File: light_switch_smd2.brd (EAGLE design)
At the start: 36.6 x 44.7 mm, 17 parts, among them J2 SW1, T1 BT136, U1 LM1117

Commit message: version 3, several correction added
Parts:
- AC: value (none) -> AC
- LAMP: value (none) -> LAMP
- moved LAMP 2.00 mm to (31.0, 42.0)
- moved AC 1.50 mm to (0.80, 41.9)
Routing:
- net N$11: track 49.5 -> 52.1 mm
- net N$8: track 36.3 -> 38.3 mm
- net GND: track 73.0 -> 73.5 mm
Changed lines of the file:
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@@
 <grid distance="0.5" unitdist="mm" unit="mm" style="lines" multiple="1" display="yes" altdistance="0.25" altunitdist="mm" altunit="mm"/>
 <layers>
-<layer number="1" name="Top" color="4" fill="1" visible="no" active="yes"/>
-<layer number="16" name="Bottom" color="1" fill="1" visible="no" active="yes"/>
+<layer number="1" name="Top" color="4" fill="1" visible="yes" active="yes"/>
+<layer number="16" name="Bottom" color="1" fill="1" visible="yes" active="yes"/>
 <layer number="17" name="Pads" color="2" fill="1" visible="yes" active="yes"/>
 <layer number="18" name="Vias" color="2" fill="1" visible="yes" active="yes"/>
@@
 <attribute name="PROD_ID" value="VREG-08170" x="12.58" y="32.06" size="1.778" layer="27" display="off"/>
 </element>
-<element name="LAMP" library="SparkFun-Connectors" package="1X03_NO_SILK" value="" x="29" y="42"/>
-<element name="AC" library="SparkFun-Connectors" package="1X03_NO_SILK" value="" x="2.3" y="41.9"/>
+<element name="LAMP" library="SparkFun-Connectors" package="1X03_NO_SILK" value="LAMP" x="31" y="42"/>
+<element name="AC" library="SparkFun-Connectors" package="1X03_NO_SILK" value="AC" x="0.8" y="41.9"/>
 </elements>
 <signals>
@@
 <wire x1="2" y1="19.4" x2="2" y2="16.21" width="0.4064" layer="16"/>
 <wire x1="2" y1="16.21" x2="2.02" y2="16.19" width="0.4064" layer="16"/>
-<wire x1="33.49" y1="3.77" x2="33.49" y2="14.21" width="0.4064" layer="16"/>
+<wire x1="33.49" y1="3.27" x2="33.49" y2="14.21" width="0.4064" layer="16"/>
 <wire x1="33.49" y1="14.21" x2="25" y2="22.7" width="0.4064" layer="16"/>
 <wire x1="25" y1="22.7" x2="8.3" y2="22.7" width="0.4064" layer="16"/>
@@
 <wire x1="23.61" y1="38.92" x2="23.61" y2="40.21" width="0.4064" layer="16"/>
 <wire x1="23.61" y1="40.21" x2="25.4" y2="42" width="0.4064" layer="16"/>
-<wire x1="25.4" y1="42" x2="29" y2="42" width="0.4064" layer="16"/>
+<wire x1="25.4" y1="42" x2="31" y2="42" width="0.4064" layer="16"/>
 </signal>
 <signal name="N$11">
@@
 <contactref element="LAMP" pad="3"/>
 <contactref element="AC" pad="1"/>
-<wire x1="2.3" y1="41.9" x2="2.3" y2="40.5" width="0.4064" layer="16"/>
-<wire x1="2.3" y1="40.5" x2="1.2" y2="39.4" width="0.4064" layer="16"/>
+<wire x1="0.8" y1="41.9" x2="0.8" y2="40.5" width="0.4064" layer="16"/>
+<wire x1="0.8" y1="40.5" x2="1.2" y2="39.4" width="0.4064" layer="16"/>
 <wire x1="1.2" y1="39.4" x2="1.2" y2="35.5" width="0.4064" layer="16"/>
 <wire x1="1.2" y1="35.5" x2="2.5" y2="34.2" width="0.4064" layer="16"/>
 <wire x1="2.5" y1="34.2" x2="23.85" y2="34.2" width="0.4064" layer="16"/>
-<wire x1="23.85" y1="34.2" x2="23.94" y2="34.29" width="0.4064" layer="16"/>
-<wire x1="23.94" y1="34.29" x2="23.94" y2="34.26" width="0.4064" layer="16"/>
-<wire x1="23.94" y1="34.26" x2="26.2" y2="32" width="0.4064" layer="16"/>
-<wire x1="26.2" y1="32" x2="31.1" y2="32" width="0.4064" layer="16"/>
-<wire x1="31.1" y1="32" x2="34.1" y2="35" width="0.4064" layer="16"/>
-<wire x1="34.1" y1="35" x2="34.1" y2="41.98" width="0.4064" layer="16"/>
-<wire x1="34.1" y1="41.98" x2="34.08" y2="42" width="0.4064" layer="16"/>
+<wire x1="23.85" y1="34.2" x2="23.94" y2="34.79" width="0.4064" layer="16"/>
+<wire x1="23.94" y1="34.79" x2="23.94" y2="33.56" width="0.4064" layer="16"/>
+<wire x1="23.94" y1="33.56" x2="26.5" y2="31" width="0.4064" layer="16"/>
+<wire x1="26.5" y1="31" x2="30" y2="31" width="0.4064" layer="16"/>
+<wire x1="30" y1="31" x2="36" y2="37" width="0.4064" layer="16"/>
+<wire x1="36" y1="37" x2="36" y2="41.92" width="0.4064" layer="16"/>
+<wire x1="36" y1="41.92" x2="36.08" y2="42" width="0.4064" layer="16"/>
 </signal>
 <signal name="N$12">
@@
 <contactref element="U$1" pad="AC1"/>
 <contactref element="AC" pad="3"/>
-<wire x1="28.42" y1="34.29" x2="28.42" y2="36.65" width="0.4064" layer="16"/>
+<wire x1="28.42" y1="34.79" x2="28.42" y2="36.65" width="0.4064" layer="16"/>
 <wire x1="28.42" y1="36.65" x2="26.15" y2="38.92" width="0.4064" layer="16"/>
-<wire x1="7.38" y1="41.9" x2="10.1" y2="41.9" width="0.4064" layer="1"/>
-<wire x1="10.1" y1="41.9" x2="16.3" y2="35.7" width="0.4064" layer="1"/>
-<wire x1="16.3" y1="35.7" x2="25" y2="35.7" width="0.4064" layer="1"/>
-<wire x1="25" y1="35.7" x2="26.2" y2="36.9" width="0.4064" layer="1"/>
+<wire x1="5.88" y1="41.9" x2="10.1" y2="41.9" width="0.4064" layer="1"/>
+<wire x1="10.1" y1="41.9" x2="16.3" y2="36.2" width="0.4064" layer="1"/>
+<wire x1="16.3" y1="36.2" x2="25" y2="36.2" width="0.4064" layer="1"/>
+<wire x1="25" y1="36.2" x2="26.2" y2="36.9" width="0.4064" layer="1"/>
 <wire x1="26.2" y1="36.9" x2="26.2" y2="38.87" width="0.4064" layer="1"/>
 <wire x1="26.2" y1="38.87" x2="26.15" y2="38.92" width="0.4064" layer="1"/>
@@
 <wire x1="14.23" y1="25.17" x2="18.9" y2="20.5" width="0.4064" layer="1"/>
 <wire x1="18.9" y1="20.5" x2="18.9" y2="3.77" width="0.4064" layer="1"/>
-<wire x1="18.9" y1="3.77" x2="18.88" y2="3.75" width="0.4064" layer="1"/>
+<wire x1="18.9" y1="3.77" x2="18.88" y2="3.25" width="0.4064" layer="1"/>
 </signal>
 <signal name="N$1">

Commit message: More minor corrections.
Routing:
- net N$17: track 8.90 -> 0.00 mm
- net GND: track 73.5 -> 66.2 mm
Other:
- board text added: "Hristo Borisov Light Switch Prototype Rev. 0.3"
- board text removed: "Hristo Borisov Light Switch Rev. 0.1 Prototype"
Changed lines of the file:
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@@
 <setting verticaltext="up"/>
 </settings>
-<grid distance="0.5" unitdist="mm" unit="mm" style="lines" multiple="1" display="yes" altdistance="0.25" altunitdist="mm" altunit="mm"/>
+<grid distance="0.1" unitdist="mm" unit="mm" style="lines" multiple="1" display="yes" altdistance="0.01" altunitdist="mm" altunit="mm"/>
 <layers>
-<layer number="1" name="Top" color="4" fill="1" visible="yes" active="yes"/>
+<layer number="1" name="Top" color="4" fill="1" visible="no" active="yes"/>
 <layer number="16" name="Bottom" color="1" fill="1" visible="yes" active="yes"/>
 <layer number="17" name="Pads" color="2" fill="1" visible="yes" active="yes"/>
@@
 <wire x1="36.6" y1="43.7" x2="0.1" y2="43.7" width="0" layer="20"/>
 <wire x1="0.1" y1="43.7" x2="0" y2="-1" width="0" layer="20"/>
-<dimension x1="0.1" y1="-1" x2="36.7" y2="-1" x3="18.4" y3="-5.4" textsize="1.778" layer="16"/>
-<text x="23.3" y="5.4" size="1.778" layer="16" rot="MR90">Hristo Borisov
-Light Switch
-Rev. 0.1 Prototype</text>
 <hole x="17.4" y="41" drill="3.2"/>
 <hole x="18.3" y="0.8" drill="3.2"/>
+<text x="32" y="26" size="1.778" layer="16" rot="MR270">Hristo Borisov
+Light Switch
+Prototype
+Rev. 0.3</text>
 </plain>
 <attributes>
@@
 <wire x1="11.18" y1="22.67" x2="8.33" y2="22.67" width="0.4064" layer="1"/>
 <wire x1="8.33" y1="22.67" x2="8.2" y2="22.8" width="0.4064" layer="1"/>
-<via x="8.2" y="22.8" extent="1-16" drill="0.6"/>
-<wire x1="8.2" y1="22.8" x2="5.4" y2="22.8" width="0.4064" layer="16"/>
-<wire x1="5.4" y1="22.8" x2="2" y2="19.4" width="0.4064" layer="16"/>
-<wire x1="2" y1="19.4" x2="2" y2="16.21" width="0.4064" layer="16"/>
-<wire x1="2" y1="16.21" x2="2.02" y2="16.19" width="0.4064" layer="16"/>
-<wire x1="33.49" y1="3.27" x2="33.49" y2="14.21" width="0.4064" layer="16"/>
-<wire x1="33.49" y1="14.21" x2="25" y2="22.7" width="0.4064" layer="16"/>
-<wire x1="25" y1="22.7" x2="8.3" y2="22.7" width="0.4064" layer="16"/>
-<wire x1="8.3" y1="22.7" x2="8.2" y2="22.8" width="0.4064" layer="16"/>
 <wire x1="2.02" y1="16.19" x2="2.02" y2="6.68" width="0.4064" layer="16"/>
 <wire x1="2.02" y1="6.68" x2="4.14" y2="4.56" width="0.4064" layer="16"/>
@@
 <vertex x="-2.5" y="-3.5"/>
 </polygon>
+<via x="8.2" y="22.8" extent="1-16" drill="0.8"/>
+<wire x1="33.49" y1="3.27" x2="22.23" y2="3.27" width="0.4064" layer="16"/>
+<wire x1="22.23" y1="3.27" x2="18.8" y2="6.7" width="0.4064" layer="16"/>
+<wire x1="18.8" y1="6.7" x2="18.8" y2="22.3" width="0.4064" layer="16"/>
+<wire x1="18.8" y1="22.3" x2="19.2" y2="22.7" width="0.4064" layer="16"/>
+<wire x1="19.2" y1="22.7" x2="8.3" y2="22.7" width="0.4064" layer="16"/>
+<wire x1="8.3" y1="22.7" x2="8.2" y2="22.8" width="0.4064" layer="16"/>
 </signal>
 <signal name="N$3">
@@
 <wire x1="6.7" y1="2" x2="6.68" y2="2.02" width="0.4064" layer="16"/>
 </signal>
-<signal name="N$17">
-<wire x1="36.6" y1="-10.2" x2="36.5" y2="-1.3" width="0.4064" layer="16"/>
-</signal>
-<signal name="N$16">
-<via x="8.2" y="22.8" extent="1-16" drill="0.8"/>
-</signal>
 <signal name="N$15">

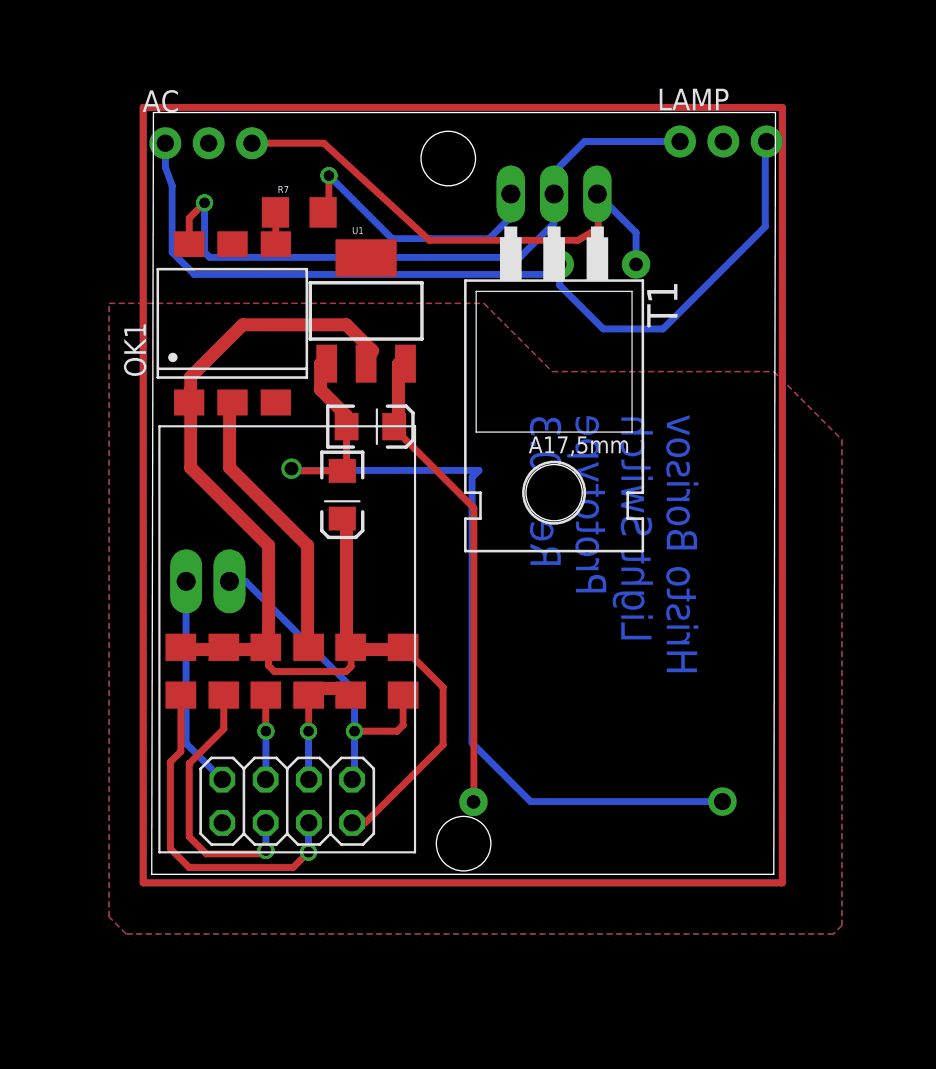
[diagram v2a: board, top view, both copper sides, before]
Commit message: pcb v4: distance between power supply pins corrected.\nSeveral vias added.
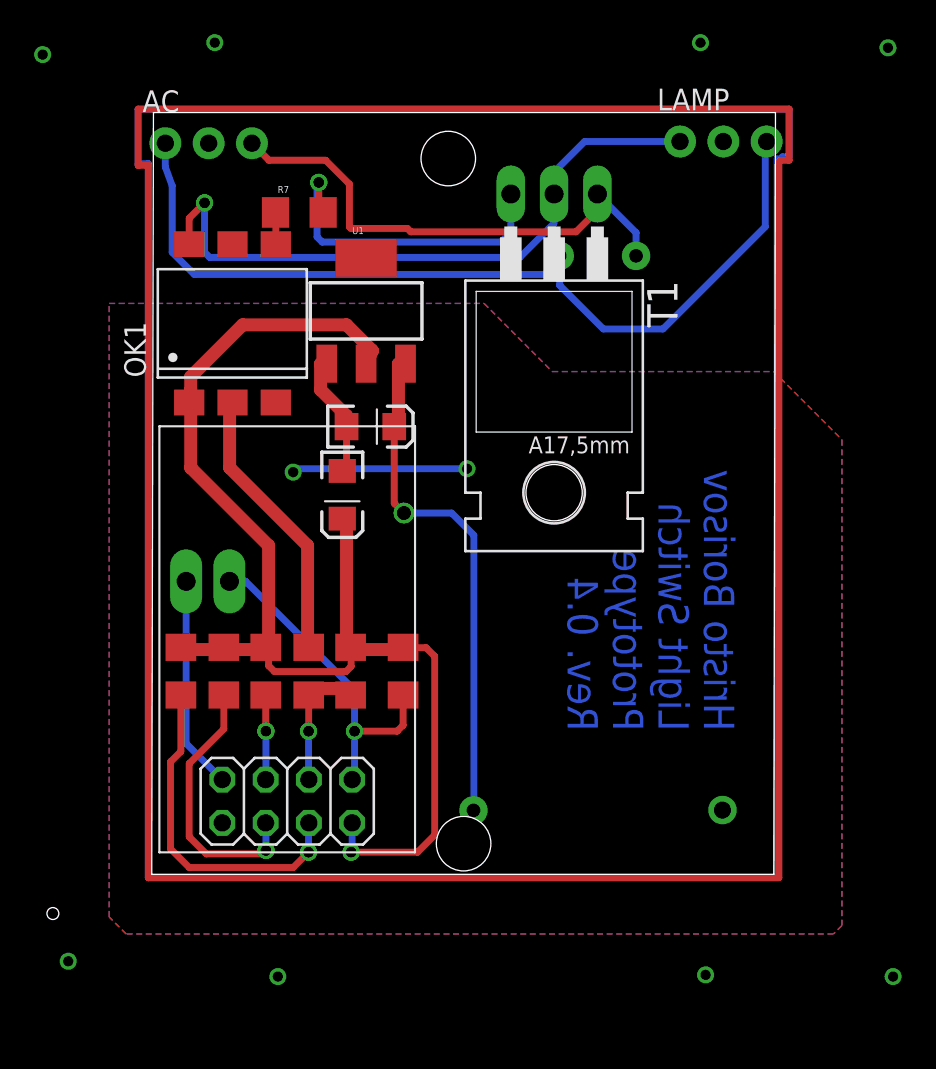
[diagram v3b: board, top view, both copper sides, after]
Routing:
- net N$32: track 0.00 -> 166.4 mm
- net N$31: track 0.00 -> 166.3 mm
- net N$24: track 166.0 -> 0.00 mm, vias 0 -> 1
- net N$10: track 166.0 -> 0.00 mm, vias 0 -> 1
- net GND: track 66.2 -> 30.2 mm, vias 1 -> 2
- net N$3: track 69.1 -> 74.8 mm, vias 0 -> 1
- net N$6: track 16.4 -> 19.1 mm
- net N$13: track 28.1 -> 30.2 mm, vias 0 -> 1
- net N$11: track 52.1 -> 53.1 mm
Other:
- board text added: "Hristo Borisov Light Switch Prototype Rev. 0.4"
- board text removed: "Hristo Borisov Light Switch Prototype Rev. 0.3"
